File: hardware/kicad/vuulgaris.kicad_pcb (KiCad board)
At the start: 2 copper layers, 284.3 x 125 mm, 46 parts, among them J1 TFPUSH, J10 PJ-603_C41409498, J2 PJ-376, J3 PJ-376, J4 PJ-376, J5 PJ-376, J7 PJ-603_C41409498, J8 PJ-603_C41409498, J9 PJ-603_C41409498, SW4 CPG151101S03, SW5 CPG151101S03, SW6 CPG151101S03, SW7 CPG151101S03, U1 ES_DAISY_PATCH_SM_REV1, U3 MCP23017-E_SO, U4 MCP23017-E_SO, U5 AMS1117-3.3, U6 AMS1117-3.3

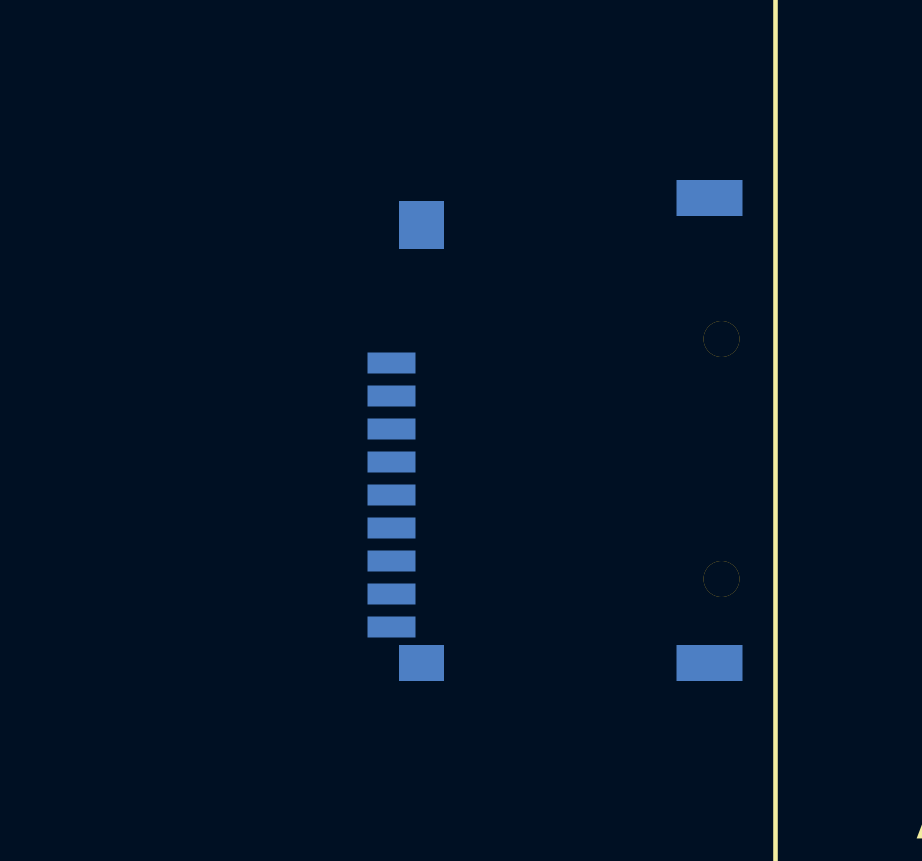
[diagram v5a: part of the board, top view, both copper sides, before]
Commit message: hardware: SD slot faces up, so the card drops in from above
J1 rotated to 0 on the back, which points the slot at the top edge. Rotating also
swaps the socket's aspect -- 15mm wide becomes 16.1mm -- which pushed it into U1's
pads, so it moves left to x232 with 4.41mm of clearance.

Costs about 7mm on the SD traces, worst case 42.7 -> 50.5mm. Acceptable for 1-bit
SDMMC over a ground plane.

Checked that the card can actually go in: an 11mm-wide path with 18mm of travel
straight up from the mouth is clear of every other back-side part. R20 and R21 lie
under that path in plan view but are on the front face, so the card rides past
them.

Back-side rotation rule again: the transform is front(lx, -ly), so rot 0 sends the
slot to -Y. Pad angles are fp_angle MINUS the library angle.
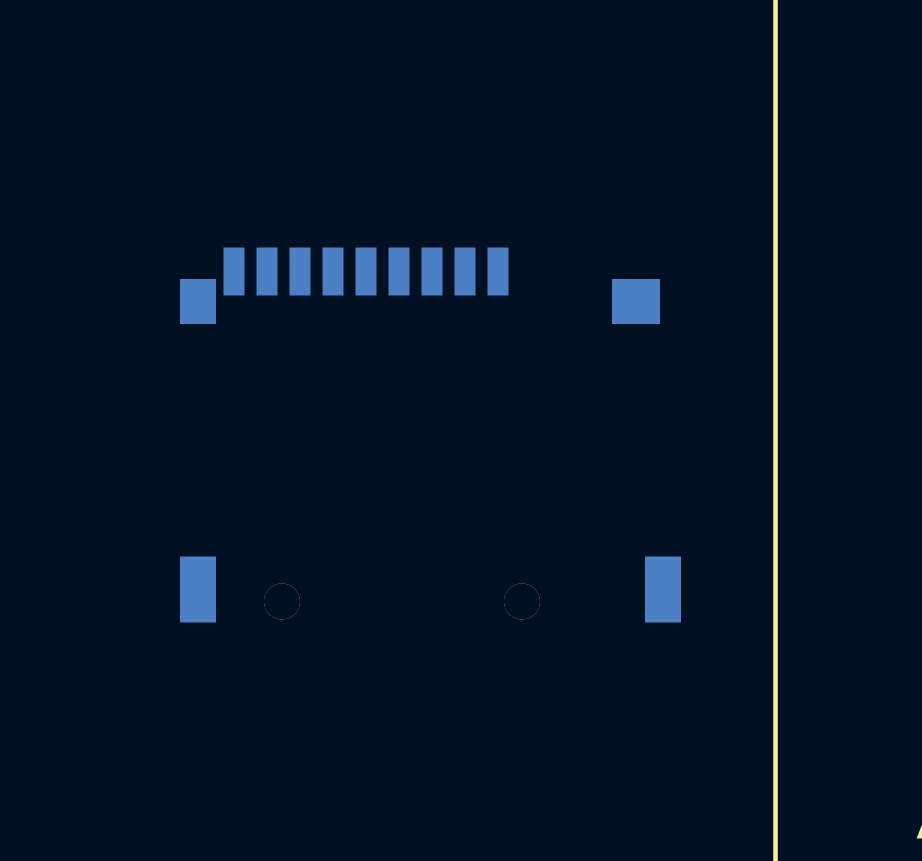
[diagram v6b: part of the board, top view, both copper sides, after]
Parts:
- moved J1 4.00 mm to (332.0, 142.0), turned to 0 degrees
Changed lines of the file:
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@@
   )
   (footprint "vuulgaris:TF-SMD_TF-PUSH" (layer "B.Cu")
-    (at 336.0 142.0 90)
+    (at 332.0 142.0)
     (property "Sheetfile" "vuulgaris.kicad_sch")
     (property "Sheetname" "")
@@
     (fp_line (start 8.07 6.09) (end 8.07 6.09)
       (stroke (width 0.05) (type solid)) (layer "B.CrtYd"))
-    (pad "" thru_hole circle (at -4.95 5.7 90) (size 1.2 1.2) (drill 1.2) (layers "*.Cu" "*.Mask"))
-    (pad "" thru_hole circle (at 3.05 5.7 90) (size 1.2 1.2) (drill 1.2) (layers "*.Cu" "*.Mask"))
-    (pad "1" smd rect (at 2.25 -5.3 90) (size 0.7 1.6) (layers "B.Cu" "B.Paste" "B.Mask")
+    (pad "" thru_hole circle (at -4.95 5.7) (size 1.2 1.2) (drill 1.2) (layers "*.Cu" "*.Mask"))
+    (pad "" thru_hole circle (at 3.05 5.7) (size 1.2 1.2) (drill 1.2) (layers "*.Cu" "*.Mask"))
+    (pad "1" smd rect (at 2.25 -5.3) (size 0.7 1.6) (layers "B.Cu" "B.Paste" "B.Mask")
       (net 65 "unconnected-(J1-DAT2-Pad1)") (pinfunction "DAT2") (pintype "unspecified+no_connect"))
-    (pad "2" smd rect (at 1.15 -5.3 90) (size 0.7 1.6) (layers "B.Cu" "B.Paste" "B.Mask")
+    (pad "2" smd rect (at 1.15 -5.3) (size 0.7 1.6) (layers "B.Cu" "B.Paste" "B.Mask")
       (net 64 "unconnected-(J1-CD{slash}DAT3-Pad2)") (pinfunction "CD/DAT3") (pintype "unspecified+no_connect"))
-    (pad "3" smd rect (at 0.05 -5.3 90) (size 0.7 1.6) (layers "B.Cu" "B.Paste" "B.Mask")
+    (pad "3" smd rect (at 0.05 -5.3) (size 0.7 1.6) (layers "B.Cu" "B.Paste" "B.Mask")
       (net 63 "/SD_CMD") (pinfunction "CMD") (pintype "unspecified"))
-    (pad "4" smd rect (at -1.05 -5.3 90) (size 0.7 1.6) (layers "B.Cu" "B.Paste" "B.Mask")
+    (pad "4" smd rect (at -1.05 -5.3) (size 0.7 1.6) (layers "B.Cu" "B.Paste" "B.Mask")
       (net 6 "/P3V3_DAISY") (pinfunction "VDD") (pintype "unspecified"))
-    (pad "5" smd rect (at -2.15 -5.3 90) (size 0.7 1.6) (layers "B.Cu" "B.Paste" "B.Mask")
+    (pad "5" smd rect (at -2.15 -5.3) (size 0.7 1.6) (layers "B.Cu" "B.Paste" "B.Mask")
       (net 62 "/SD_CLK") (pinfunction "CLX") (pintype "unspecified"))
-    (pad "6" smd rect (at -3.25 -5.3 90) (size 0.7 1.6) (layers "B.Cu" "B.Paste" "B.Mask")
+    (pad "6" smd rect (at -3.25 -5.3) (size 0.7 1.6) (layers "B.Cu" "B.Paste" "B.Mask")
       (net 1 "/GND") (pinfunction "VSS") (pintype "unspecified"))
-    (pad "7" smd rect (at -4.35 -5.3 90) (size 0.7 1.6) (layers "B.Cu" "B.Paste" "B.Mask")
+    (pad "7" smd rect (at -4.35 -5.3) (size 0.7 1.6) (layers "B.Cu" "B.Paste" "B.Mask")
       (net 61 "/SD_D0") (pinfunction "DAT0") (pintype "unspecified"))
-    (pad "8" smd rect (at -5.45 -5.3 90) (size 0.7 1.6) (layers "B.Cu" "B.Paste" "B.Mask")
+    (pad "8" smd rect (at -5.45 -5.3) (size 0.7 1.6) (layers "B.Cu" "B.Paste" "B.Mask")
       (net 60 "unconnected-(J1-DAT1-Pad8)") (pinfunction "DAT1") (pintype "unspecified+no_connect"))
-    (pad "10" smd rect (at -7.75 -4.3 90) (size 1.2 1.5) (layers "B.Cu" "B.Paste" "B.Mask")
+    (pad "10" smd rect (at -7.75 -4.3) (size 1.2 1.5) (layers "B.Cu" "B.Paste" "B.Mask")
       (net 1 "/GND") (pinfunction "10") (pintype "unspecified"))
-    (pad "11" smd rect (at -7.75 5.3 90) (size 1.2 2.2) (layers "B.Cu" "B.Paste" "B.Mask")
+    (pad "11" smd rect (at -7.75 5.3) (size 1.2 2.2) (layers "B.Cu" "B.Paste" "B.Mask")
       (net 1 "/GND") (pinfunction "11") (pintype "unspecified"))
-    (pad "12" smd rect (at 7.75 5.3 90) (size 1.2 2.2) (layers "B.Cu" "B.Paste" "B.Mask")
+    (pad "12" smd rect (at 7.75 5.3) (size 1.2 2.2) (layers "B.Cu" "B.Paste" "B.Mask")
       (net 1 "/GND") (pinfunction "12") (pintype "unspecified"))
-    (pad "13" smd rect (at 6.85 -4.3 90) (size 1.6 1.5) (layers "B.Cu" "B.Paste" "B.Mask")
+    (pad "13" smd rect (at 6.85 -4.3) (size 1.6 1.5) (layers "B.Cu" "B.Paste" "B.Mask")
       (net 1 "/GND") (pinfunction "13") (pintype "unspecified"))
-    (pad "CD" smd rect (at -6.55 -5.3 90) (size 0.7 1.6) (layers "B.Cu" "B.Paste" "B.Mask")
+    (pad "CD" smd rect (at -6.55 -5.3) (size 0.7 1.6) (layers "B.Cu" "B.Paste" "B.Mask")
       (net 66 "unconnected-(J1-PadCD)") (pinfunction "CD") (pintype "unspecified+no_connect"))
     (model "/Users/dylanhackett/V1/hardware/kicad/lib/vuulgaris.3dshapes/TF-SMD_TF-PUSH.wrl"

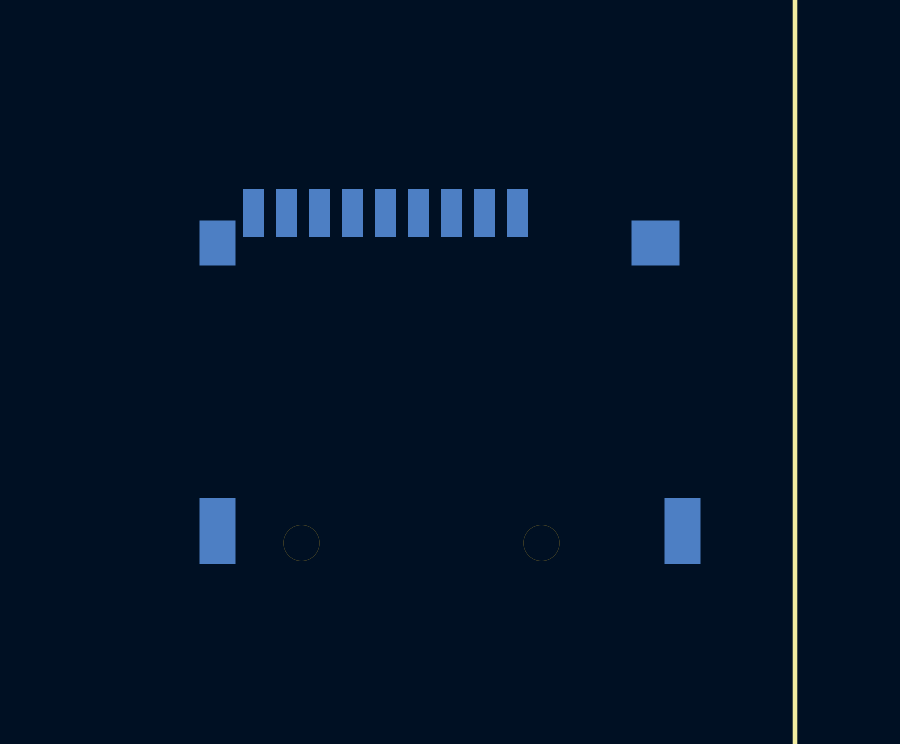
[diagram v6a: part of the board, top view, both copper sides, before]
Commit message: hardware: flip J1 180 degrees
Card entry now at the bottom of the socket, contacts at the top.

  body       y[86.70, 101.70]
  contacts   y  85.90
  entry      y 101.70

Clearances unchanged: 7.28mm to the Daisy's A header, 4.41mm to its pads in x.
156 non-circular pads at library orientation, 0 pad overlaps, all 20 panel parts
on their holes.
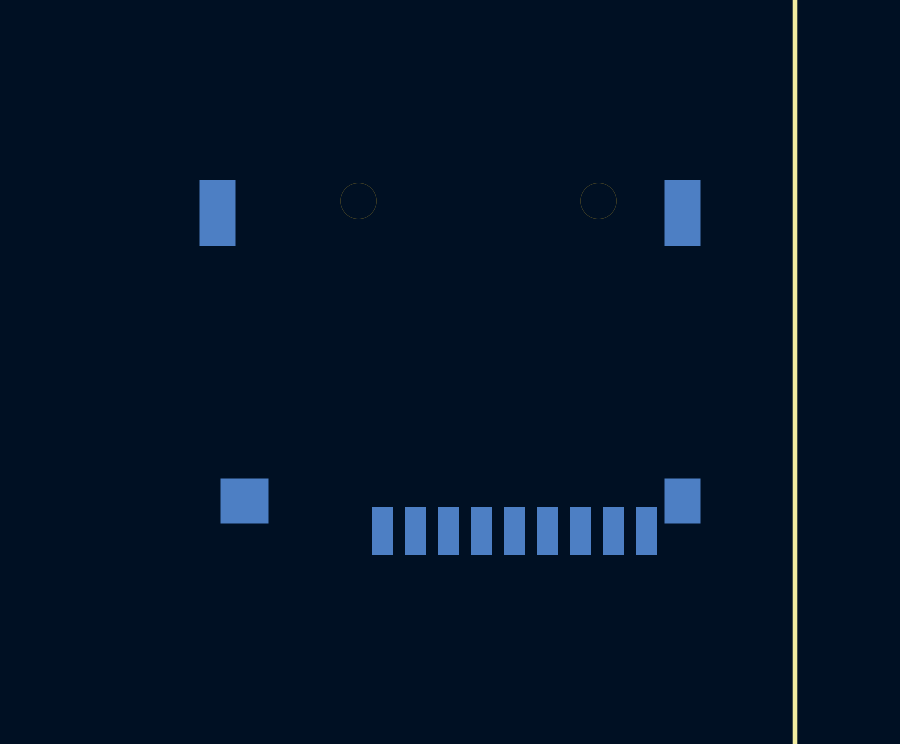
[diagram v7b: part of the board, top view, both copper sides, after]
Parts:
- turned J1 to 180 degrees
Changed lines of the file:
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@@
   )
   (footprint "vuulgaris:TF-SMD_TF-PUSH" (layer "B.Cu")
-    (at 332.0 142.0)
+    (at 332.0 142.0 180)
     (property "Sheetfile" "vuulgaris.kicad_sch")
     (property "Sheetname" "")
@@
     (fp_line (start 8.07 6.09) (end 8.07 6.09)
       (stroke (width 0.05) (type solid)) (layer "B.CrtYd"))
-    (pad "" thru_hole circle (at -4.95 5.7) (size 1.2 1.2) (drill 1.2) (layers "*.Cu" "*.Mask"))
-    (pad "" thru_hole circle (at 3.05 5.7) (size 1.2 1.2) (drill 1.2) (layers "*.Cu" "*.Mask"))
-    (pad "1" smd rect (at 2.25 -5.3) (size 0.7 1.6) (layers "B.Cu" "B.Paste" "B.Mask")
+    (pad "" thru_hole circle (at -4.95 5.7 180) (size 1.2 1.2) (drill 1.2) (layers "*.Cu" "*.Mask"))
+    (pad "" thru_hole circle (at 3.05 5.7 180) (size 1.2 1.2) (drill 1.2) (layers "*.Cu" "*.Mask"))
+    (pad "1" smd rect (at 2.25 -5.3 180) (size 0.7 1.6) (layers "B.Cu" "B.Paste" "B.Mask")
       (net 65 "unconnected-(J1-DAT2-Pad1)") (pinfunction "DAT2") (pintype "unspecified+no_connect"))
-    (pad "2" smd rect (at 1.15 -5.3) (size 0.7 1.6) (layers "B.Cu" "B.Paste" "B.Mask")
+    (pad "2" smd rect (at 1.15 -5.3 180) (size 0.7 1.6) (layers "B.Cu" "B.Paste" "B.Mask")
       (net 64 "unconnected-(J1-CD{slash}DAT3-Pad2)") (pinfunction "CD/DAT3") (pintype "unspecified+no_connect"))
-    (pad "3" smd rect (at 0.05 -5.3) (size 0.7 1.6) (layers "B.Cu" "B.Paste" "B.Mask")
+    (pad "3" smd rect (at 0.05 -5.3 180) (size 0.7 1.6) (layers "B.Cu" "B.Paste" "B.Mask")
       (net 63 "/SD_CMD") (pinfunction "CMD") (pintype "unspecified"))
-    (pad "4" smd rect (at -1.05 -5.3) (size 0.7 1.6) (layers "B.Cu" "B.Paste" "B.Mask")
+    (pad "4" smd rect (at -1.05 -5.3 180) (size 0.7 1.6) (layers "B.Cu" "B.Paste" "B.Mask")
       (net 6 "/P3V3_DAISY") (pinfunction "VDD") (pintype "unspecified"))
-    (pad "5" smd rect (at -2.15 -5.3) (size 0.7 1.6) (layers "B.Cu" "B.Paste" "B.Mask")
+    (pad "5" smd rect (at -2.15 -5.3 180) (size 0.7 1.6) (layers "B.Cu" "B.Paste" "B.Mask")
       (net 62 "/SD_CLK") (pinfunction "CLX") (pintype "unspecified"))
-    (pad "6" smd rect (at -3.25 -5.3) (size 0.7 1.6) (layers "B.Cu" "B.Paste" "B.Mask")
+    (pad "6" smd rect (at -3.25 -5.3 180) (size 0.7 1.6) (layers "B.Cu" "B.Paste" "B.Mask")
       (net 1 "/GND") (pinfunction "VSS") (pintype "unspecified"))
-    (pad "7" smd rect (at -4.35 -5.3) (size 0.7 1.6) (layers "B.Cu" "B.Paste" "B.Mask")
+    (pad "7" smd rect (at -4.35 -5.3 180) (size 0.7 1.6) (layers "B.Cu" "B.Paste" "B.Mask")
       (net 61 "/SD_D0") (pinfunction "DAT0") (pintype "unspecified"))
-    (pad "8" smd rect (at -5.45 -5.3) (size 0.7 1.6) (layers "B.Cu" "B.Paste" "B.Mask")
+    (pad "8" smd rect (at -5.45 -5.3 180) (size 0.7 1.6) (layers "B.Cu" "B.Paste" "B.Mask")
       (net 60 "unconnected-(J1-DAT1-Pad8)") (pinfunction "DAT1") (pintype "unspecified+no_connect"))
-    (pad "10" smd rect (at -7.75 -4.3) (size 1.2 1.5) (layers "B.Cu" "B.Paste" "B.Mask")
+    (pad "10" smd rect (at -7.75 -4.3 180) (size 1.2 1.5) (layers "B.Cu" "B.Paste" "B.Mask")
       (net 1 "/GND") (pinfunction "10") (pintype "unspecified"))
-    (pad "11" smd rect (at -7.75 5.3) (size 1.2 2.2) (layers "B.Cu" "B.Paste" "B.Mask")
+    (pad "11" smd rect (at -7.75 5.3 180) (size 1.2 2.2) (layers "B.Cu" "B.Paste" "B.Mask")
       (net 1 "/GND") (pinfunction "11") (pintype "unspecified"))
-    (pad "12" smd rect (at 7.75 5.3) (size 1.2 2.2) (layers "B.Cu" "B.Paste" "B.Mask")
+    (pad "12" smd rect (at 7.75 5.3 180) (size 1.2 2.2) (layers "B.Cu" "B.Paste" "B.Mask")
       (net 1 "/GND") (pinfunction "12") (pintype "unspecified"))
-    (pad "13" smd rect (at 6.85 -4.3) (size 1.6 1.5) (layers "B.Cu" "B.Paste" "B.Mask")
+    (pad "13" smd rect (at 6.85 -4.3 180) (size 1.6 1.5) (layers "B.Cu" "B.Paste" "B.Mask")
       (net 1 "/GND") (pinfunction "13") (pintype "unspecified"))
-    (pad "CD" smd rect (at -6.55 -5.3) (size 0.7 1.6) (layers "B.Cu" "B.Paste" "B.Mask")
+    (pad "CD" smd rect (at -6.55 -5.3 180) (size 0.7 1.6) (layers "B.Cu" "B.Paste" "B.Mask")
       (net 66 "unconnected-(J1-PadCD)") (pinfunction "CD") (pintype "unspecified+no_connect"))
     (model "/Users/dylanhackett/V1/hardware/kicad/lib/vuulgaris.3dshapes/TF-SMD_TF-PUSH.wrl"

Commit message: hardware: power input stage — 12V barrel in, -12V from a flipped isolated module
POS12V and NEG12V had one node each (U1.A5, U1.A1) and nothing driving them. This
fills that.

+12V comes straight off the barrel. The negative rail uses a 1W isolated 12V-to-12V
module with its +Vout tied to ground, so the floating output sits at -12V. Topology
follows mesotokyo/cheap-power-board (CC-BY 4.0), which does the same with a 10W TDK
CC10; the forced deviations are no NJM2396 (12V in leaves no headroom to
linear-regulate +12V), no LM7805 (the Daisy supplies 5V), the far smaller module,
and a bleeder their part does not need.

  J11  DC-005-20A         C130239   $0.14
  D1   SS34 series        C8678     $0.03
  C28  470uF/25V Rubycon  C88740    $0.15
  U7   B1212S-1WR3        C3031174  $0.93
  L1/L2 4.7uH             C139243   $0.09
  D2/D3 SS34 shunt clamps, C29-C32 filter, R22-R24 bleeder
                                             about $1.39 against $15.36

Four pinouts verified against datasheets, not inferred. SS34 has pin 1 as CATHODE,
the reverse of the usual convention -- wiring it by assumption puts a forward diode
across the supply. DC-005-A is 1=tip, 2=sleeve, 3=switch. B1212S is 1=-Vin, 2=+Vin,
3=-Vout, 4=+Vout. The electrolytic's silk band sits on pad 2, so pad 1 is positive.

The bleeder exists because the module needs 10% of rated (8.4mA) as minimum load,
and the -12V draw is only 5mA for the Patch SM plus 3-6mA of LPG op-amps. Three 2.2k
0402s in series rather than one, because the datasheet wants the resistor rated at
5x its dissipation and a single 2.2k dissipates 65mW in a 62.5mW part.

Schematic: 61 components, 192 connections, 63 nets, VERIFIED 192/192 with 0
unintended. UNTESTED in hardware -- the check confirms the board matches netmap.json,
not that netmap.json is correct. Breadboard before fab.
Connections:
- U1 pad B9: /ENC0_PUSH -> unconnected-(U1-GATE_IN_2-PadB9)
- U1 pad D3: /ENC0_A -> unconnected-(U1-SDMMC_D2-PadD3)
- U1 pad D4: /ENC0_B -> unconnected-(U1-SDMMC_D1-PadD4)
- U4 pad 1: unconnected-(U4-GPB0-Pad1) -> /ENC0_A
- U4 pad 2: unconnected-(U4-GPB1-Pad2) -> /ENC0_B
- U4 pad 3: unconnected-(U4-GPB2-Pad3) -> /ENC0_PUSH
